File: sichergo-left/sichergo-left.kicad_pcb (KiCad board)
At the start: 2 copper layers, 111.5 x 103.1 mm, 111 parts, among them J1 Conn_01x04_Pin, Q1 2N7002, SW1 SW_Push, SW10 SW_Push, SW11 SW_Push, SW12 SW_Push, SW13 SW_Push, SW14 SW_Push, SW15 SW_Push, SW16 SW_Push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

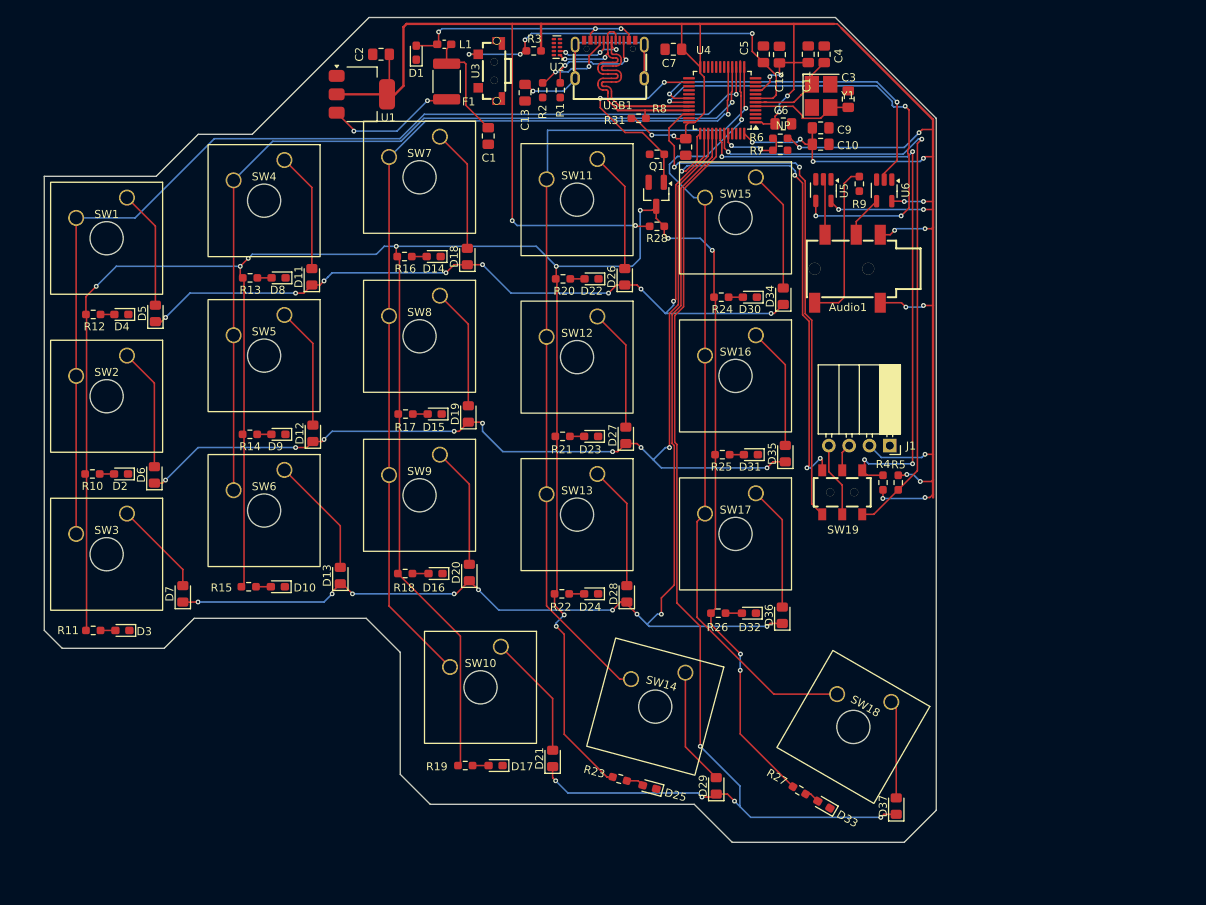
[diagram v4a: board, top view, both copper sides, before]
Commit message: Finish routing LEFT side
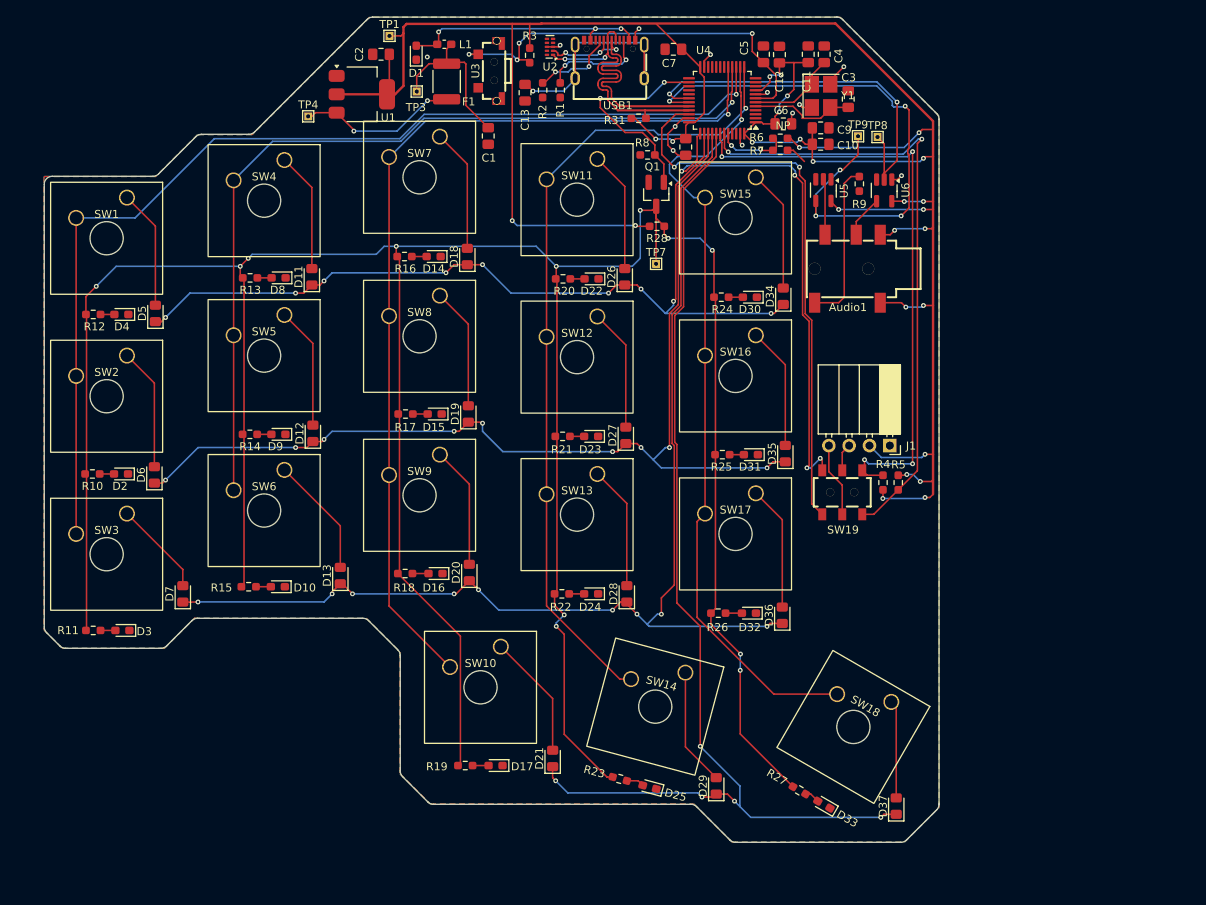
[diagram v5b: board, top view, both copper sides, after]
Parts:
- added TP1: TestPoint, TestPoint:TestPoint_THTPad_1.0x1.0mm_Drill0.5mm, F.Cu at (133.7, 53.7)
- added TP3: TestPoint, TestPoint:TestPoint_THTPad_1.0x1.0mm_Drill0.5mm, F.Cu at (137.1, 60.7)
- added TP4: TestPoint, TestPoint:TestPoint_THTPad_1.0x1.0mm_Drill0.5mm, F.Cu at (123.5, 63.8)
- added TP7: TestPoint, TestPoint:TestPoint_THTPad_1.0x1.0mm_Drill0.5mm, F.Cu at (167.0, 82.2)
- added TP8: TestPoint, TestPoint:TestPoint_THTPad_1.0x1.0mm_Drill0.5mm, F.Cu at (194.7, 66.3)
- added TP9: TestPoint, TestPoint:TestPoint_THTPad_1.0x1.0mm_Drill0.5mm, F.Cu at (192.2, 66.2)
- moved R8 1.18 mm to (165.9, 68.6)
- moved U2 0.86 mm to (153.7, 55.1)
- moved R3 0.76 mm to (151.2, 56.1), turned to -90 degrees
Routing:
- net GND: track 0.00 -> 25.7 mm, vias 0 -> 12
- net /UART_RX: track 61.2 -> 73.5 mm, vias 4 -> 5
- net +3V3: track 342.9 -> 336.5 mm
- net Net-(C1-Pad1): track 14.4 -> 20.4 mm
- net /UART_TX: track 43.1 -> 48.8 mm
- net Net-(U1-VI): track 16.4 -> 19.9 mm
- net /KB_COL_3: track 105.1 -> 102.0 mm
- net Net-(U4-NRST): track 50.4 -> 52.7 mm
- net /D-: track 36.0 -> 37.3 mm
- net /SWDIO: track 69.0 -> 70.3 mm
- net /MatrixL/LED_DRIVE: track 383.8 -> 385.0 mm
- net Net-(C13-Pad1): track 24.6 -> 23.6 mm
- net Net-(D37-A): track 12.3 -> 11.4 mm
- net /KB_COL_4: track 100.0 -> 99.3 mm
- net /D+: track 36.6 -> 37.3 mm
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- added copper zone on B.Cu, net GND
- added copper zone on F.Cu, net GND
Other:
- board size 111.5 x 103.1 mm -> 111.8 x 103.2 mm

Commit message: Remake entire shape
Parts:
- moved D1 102.9 mm to (223.7, 111.1), turned to -120 degrees
- moved TP4 100.9 mm to (213.6, 109.1), turned to 60 degrees
- moved L1 96.9 mm to (220.6, 109.3), turned to 60 degrees
- moved C5 95.3 mm to (120.9, 130.5), turned to -90 degrees
- moved C2 92.0 mm to (203.4, 114.7), turned to -120 degrees
- moved TP3 90.7 mm to (212.4, 111.2), turned to 60 degrees
- moved U1 90.3 mm to (206.6, 109.1), turned to 60 degrees
- moved F1 90.1 mm to (217.2, 107.0), turned to 150 degrees
- moved C1 87.9 mm to (222.2, 110.0), turned to -120 degrees
- moved U2 86.9 mm to (211.3, 120.1), turned to -120 degrees
- moved TP1 86.5 mm to (204.1, 103.8), turned to 60 degrees
- moved R2 85.6 mm to (209.2, 124.9)
- moved R1 85.3 mm to (210.8, 124.9)
- moved C13 82.9 mm to (207.7, 120.9)
- moved USB1 81.3 mm to (217.0, 115.8), turned to -120 degrees
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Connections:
- R28 pad 1: /MatrixL/LED_DRIVE -> +3V3
- R28 pad 2: +3V3 -> /MatrixL/LED_DRIVE
- U4 pad 18: unconnected-(U4-PB0-Pad18) -> /KB_ROW_1
- U4 pad 19: unconnected-(U4-PB1-Pad19) -> /KB_ROW_2
- U4 pad 20: unconnected-(U4-PB2-Pad20) -> /KB_ROW_3
- U4 pad 21: unconnected-(U4-PB10-Pad21) -> /KB_ROW_0
- U4 pad 38: /KB_ROW_0 -> unconnected-(U4-PA15-Pad38)
- U4 pad 39: /KB_ROW_1 -> unconnected-(U4-PB3-Pad39)
- U4 pad 40: /KB_ROW_2 -> unconnected-(U4-PB4-Pad40)
- U4 pad 41: /KB_ROW_3 -> unconnected-(U4-PB5-Pad41)
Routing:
- net /MatrixL/LED_DRIVE: track 385.0 -> 0.00 mm, vias 12 -> 0
- net +3V3: track 336.5 -> 0.00 mm, vias 27 -> 0
- net /KB_ROW_2: track 145.4 -> 0.00 mm, vias 9 -> 0
- net /KB_ROW_3: track 136.0 -> 0.00 mm, vias 5 -> 0
- net /KB_COL_0: track 131.8 -> 0.00 mm, vias 1 -> 0
- net /KB_ROW_1: track 130.0 -> 0.00 mm, vias 9 -> 0
- net /KB_COL_2: track 117.4 -> 0.00 mm, vias 1 -> 0
- net /KB_ROW_0: track 109.8 -> 0.00 mm, vias 9 -> 0
- net /KB_COL_1: track 109.6 -> 0.00 mm, vias 1 -> 0
- net /KB_COL_3: track 102.0 -> 0.00 mm, vias 1 -> 0
- net /KB_COL_4: track 99.3 -> 0.00 mm, vias 1 -> 0
- net /OLED_SDA: track 78.4 -> 0.00 mm, vias 2 -> 0
- net /OLED_SCL: track 76.2 -> 0.00 mm, vias 4 -> 0
- net /UART_RX: track 73.5 -> 0.00 mm, vias 5 -> 0
- net /SWDIO: track 70.3 -> 0.00 mm, vias 2 -> 0
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- removed copper zone on B.Cu, net GND
- removed copper zone on F.Cu, net GND
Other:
- board size 111.8 x 103.2 mm -> 116.6 x 96.1 mm
- board text added: "Daniel (steewBSD)"

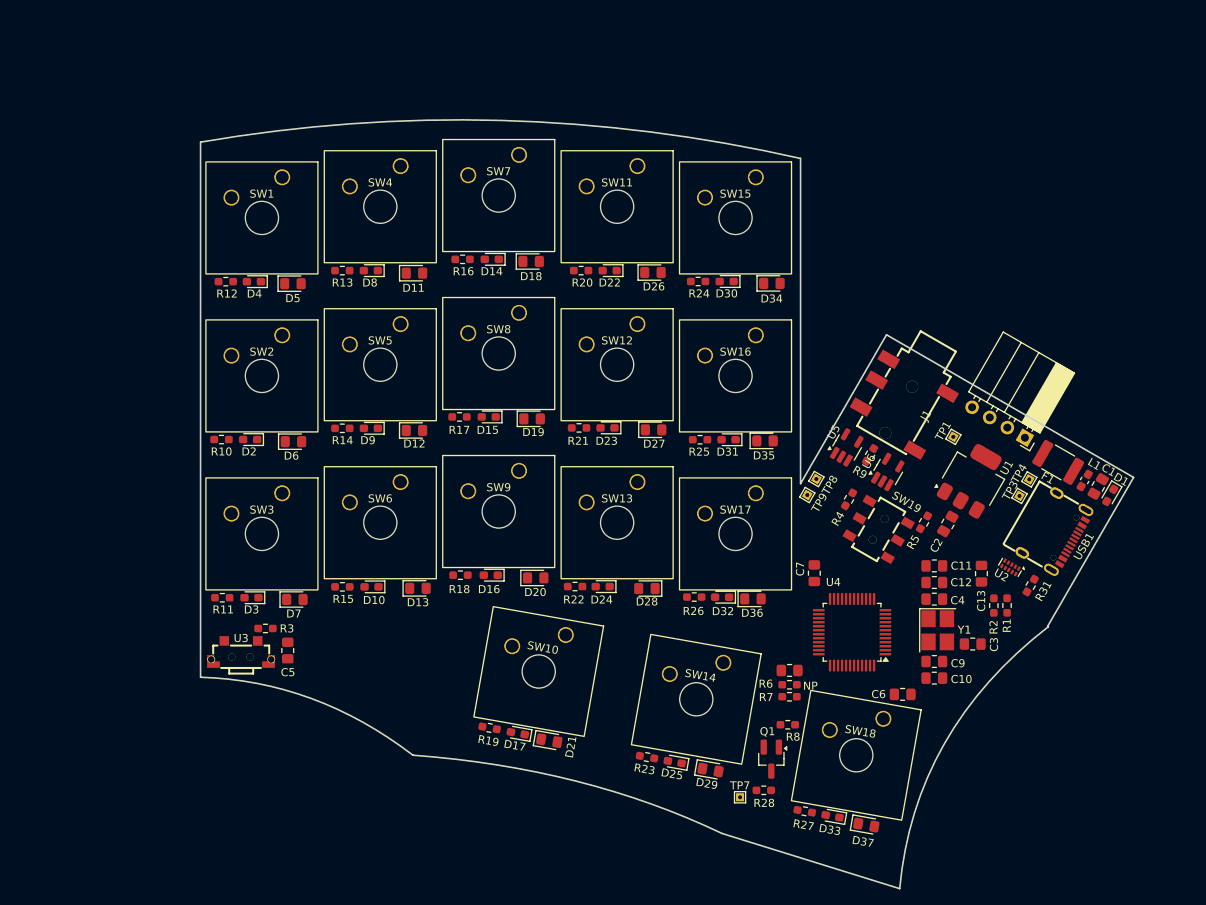
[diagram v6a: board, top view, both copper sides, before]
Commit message: Finish routing new LEFT
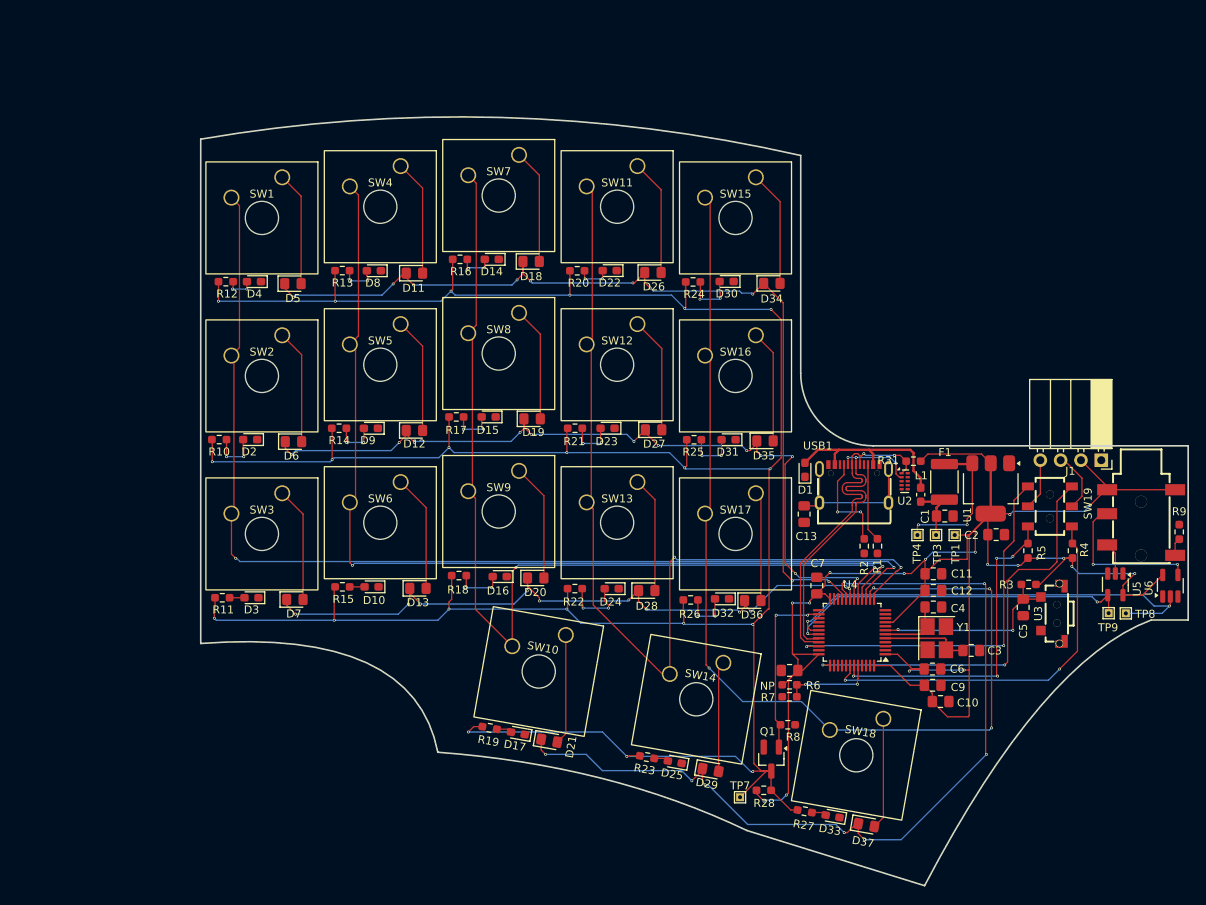
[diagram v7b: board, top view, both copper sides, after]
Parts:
- moved U3 101.4 mm to (216.4, 125.9), turned to 90 degrees
- moved R3 95.6 mm to (213.6, 122.3)
- moved C5 92.1 mm to (212.9, 125.1)
- moved TP8 42.2 mm to (225.7, 125.9), turned to 0 degrees
- moved TP9 40.5 mm to (223.6, 125.9), turned to 0 degrees
- moved R9 39.8 mm to (232.4, 115.7), turned to -90 degrees
- moved D1 38.3 mm to (185.6, 107.9), turned to 90 degrees
- moved U6 38.1 mm to (231.3, 122.4), turned to 90 degrees
- moved U5 37.7 mm to (224.4, 122.3), turned to -90 degrees
- moved Audio1 33.4 mm to (227.6, 114.5), turned to 180 degrees
- moved R4 28.7 mm to (219.0, 118.1), turned to 90 degrees
- moved USB1 26.0 mm to (191.7, 109.7), turned to 0 degrees
- moved C13 23.4 mm to (185.5, 113.5)
- moved SW19 21.6 mm to (216.2, 112.5), turned to -90 degrees
- moved R31 21.4 mm to (199.2, 106.9), turned to 180 degrees
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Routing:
- net /MatrixL/LED_DRIVE: track 0.00 -> 378.1 mm, vias 0 -> 21
- net +3V3: track 0.00 -> 246.4 mm, vias 0 -> 18
- net /KB_COL_0: track 0.00 -> 135.0 mm, vias 0 -> 2
- net /KB_COL_4: track 0.00 -> 132.3 mm, vias 0 -> 4
- net /KB_COL_2: track 0.00 -> 122.3 mm, vias 0 -> 2
- net /KB_COL_1: track 0.00 -> 120.7 mm, vias 0 -> 2
- net /KB_ROW_0: track 0.00 -> 116.5 mm, vias 0 -> 10
- net /KB_COL_3: track 0.00 -> 116.0 mm, vias 0 -> 2
- net /KB_ROW_3: track 0.00 -> 111.6 mm, vias 0 -> 8
- net /KB_ROW_1: track 0.00 -> 101.2 mm, vias 0 -> 12
- net /KB_ROW_2: track 0.00 -> 86.5 mm, vias 0 -> 10
- net /UART_TX: track 0.00 -> 56.5 mm, vias 0 -> 2
- net /SWCLK: track 0.00 -> 52.1 mm, vias 0 -> 2
- net /OLED_SCL: track 0.00 -> 48.5 mm, vias 0 -> 2
- net /SWDIO: track 0.00 -> 47.4 mm, vias 0 -> 2
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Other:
- board size 116.6 x 96.1 mm -> 123.4 x 96.1 mm

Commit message: Pre DRC
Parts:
- moved R4 1.45 mm to (218.9, 119.5)
- moved SW19 1.16 mm to (216.2, 113.7)
- moved R5 0.95 mm to (213.4, 119.0)
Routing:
- net +3V3: track 246.4 -> 243.0 mm, vias 18 -> 11
- net /OLED_SCL: track 48.5 -> 47.1 mm
- net Net-(J1-Pin_4): track 6.41 -> 7.59 mm
- net Net-(J1-Pin_3): track 7.66 -> 8.83 mm
- net /SWDIO: track 47.4 -> 46.2 mm
- net /SWCLK: track 52.1 -> 50.9 mm
- net /OLED_SDA: track 41.0 -> 40.3 mm
- added copper zone on B.Cu, net GND
- added copper zone on F.Cu, net GND
